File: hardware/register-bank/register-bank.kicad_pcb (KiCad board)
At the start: 2 copper layers, 51.6 x 51.6 mm, 64 parts, among them J1 Conn_Reg, J2 Conn_Power, U1 HEF4557B, U10 74HC251, U11 74HC251, U12 MIC5504-3.3YM5, U13 74LVC1G04, U14 74LVC1G04, U15 74LVC1G04, U16 74LVC1G04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

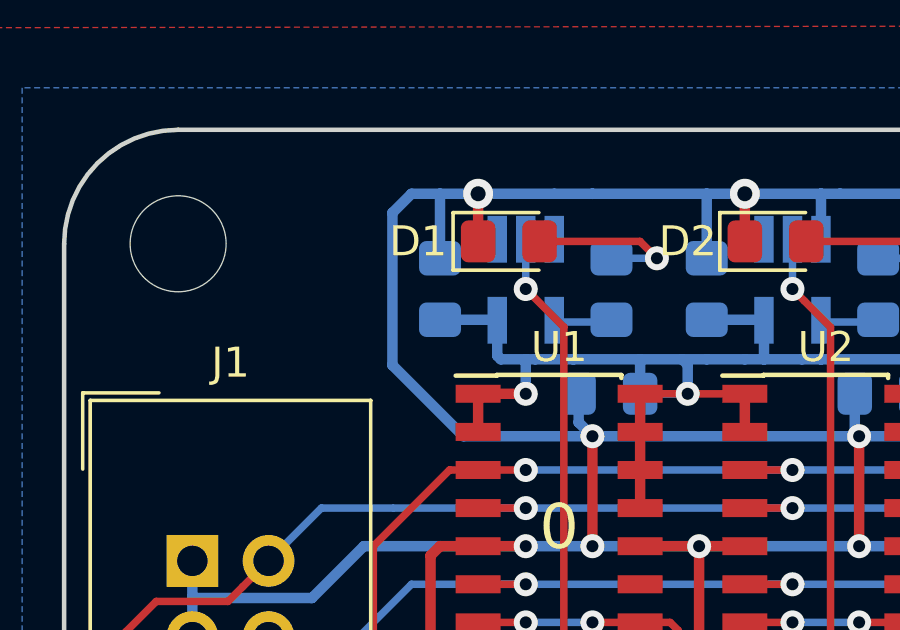
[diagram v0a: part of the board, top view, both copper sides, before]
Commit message: Added test points
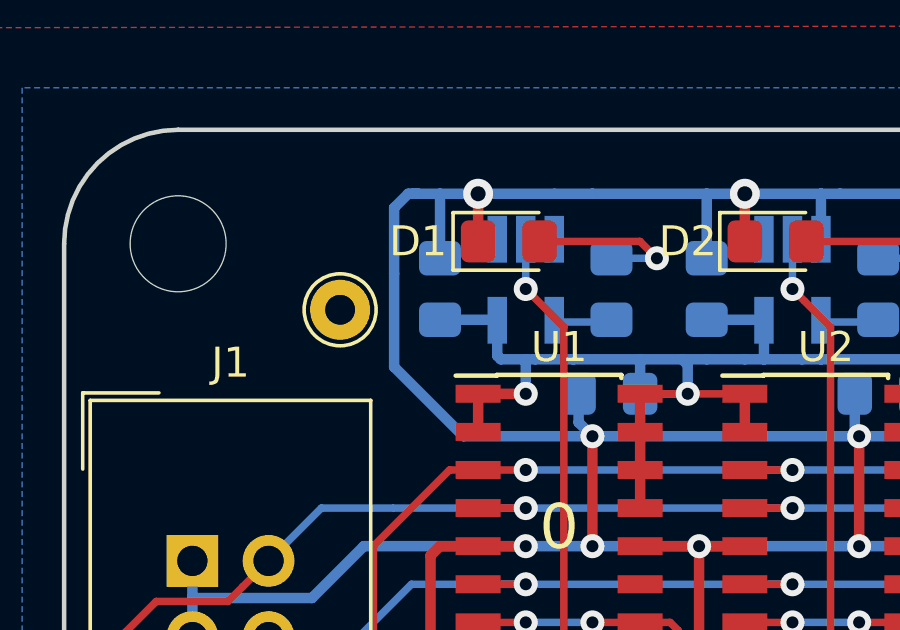
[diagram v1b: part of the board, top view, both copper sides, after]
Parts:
- added TP1: TestPoint, TestPoint:TestPoint_THTPad_D2.0mm_Drill1.0mm, F.Cu at (71.6, 73.4)
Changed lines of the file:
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@@
     (thickness 1.6)
     (drawings 19)
-    (tracks 1025)
+    (tracks 1028)
     (zones 0)
-    (modules 64)
+    (modules 65)
     (nets 72)
   )
@@
   )
   (setup
-    (last_trace_width 0.25)
+    (last_trace_width 0.35)
     (user_trace_width 0.35)
     (user_trace_width 0.5)
@@
       (xy 0.1016 -0.166391)) (layer B.SilkS) (width 0.01))
   )
+  (module TestPoint:TestPoint_THTPad_D2.0mm_Drill1.0mm (layer F.Cu)
+    (at 71.6 73.4)
+    (descr "THT pad as test Point, diameter 2.0mm, hole diameter 1.0mm")
+    (tags "test point THT pad")
+    (attr virtual)
+    (fp_text reference TP1 (at 0 -1.998) (layer F.SilkS) hide
+      (effects (font (size 1 1) (thickness 0.15)))
+    )
+    (fp_text value TestPoint (at 0 2.05) (layer F.Fab)
+      (effects (font (size 1 1) (thickness 0.15)))
+    )
+    (fp_text user %R (at 0 -2) (layer F.Fab)
+      (effects (font (size 1 1) (thickness 0.15)))
+    )
+    (fp_circle (center 0 0) (end 1.5 0) (layer F.CrtYd) (width 0.05))
+    (fp_circle (center 0 0) (end 0 1.2) (layer F.SilkS) (width 0.12))
+    (pad 1 thru_hole circle (at 0 0) (size 2 2) (drill 1) (layers *.Cu *.Mask)
+      (net 1 GND))
+  )
   (gr_text 0 (at 78.9 80.645) (layer F.SilkS)
     (effects (font (size 1.5 1.5) (thickness 0.3)))
@@
   (segment (start 87.6275 71.6075) (end 87.6275 69.535) (width 0.35) (layer B.Cu) (net 1) (status 10))
   (segment (start 87.63 69.5325) (end 88.265 69.5325) (width 0.35) (layer B.Cu) (net 1))
-  (segment (start 75.71 77.615) (end 80.01 77.615) (width 0.35) (layer B.Cu) (net 1))
-  (segment (start 73.3425 75.2475) (end 75.71 77.615) (width 0.35) (layer B.Cu) (net 1))
-  (segment (start 73.3425 70.1675) (end 73.3425 75.2475) (width 0.35) (layer B.Cu) (net 1))
-  (segment (start 74.93 69.5325) (end 73.9775 69.5325) (width 0.35) (layer B.Cu) (net 1))
-  (segment (start 73.9775 69.5325) (end 73.3425 70.1675) (width 0.35) (layer B.Cu) (net 1))
   (segment (start 111.125 76.125) (end 111.05 76.125) (width 0.35) (layer B.Cu) (net 1))
   (segment (start 104.4575 69.5325) (end 103.505 69.5325) (width 0.35) (layer B.Cu) (net 1))
@@
   (segment (start 103.255 93.345) (end 103.1875 93.345) (width 0.5) (layer B.Cu) (net 1))
   (segment (start 103.6 93) (end 103.255 93.345) (width 0.5) (layer B.Cu) (net 1))
+  (segment (start 74.93 69.5325) (end 74.2 69.5325) (width 0.35) (layer B.Cu) (net 1))
+  (segment (start 74.2 69.5325) (end 73.9775 69.5325) (width 0.35) (layer B.Cu) (net 1))
+  (segment (start 73.8675 69.5325) (end 74.2 69.5325) (width 0.35) (layer B.Cu) (net 1))
+  (segment (start 73.4 70) (end 73.8675 69.5325) (width 0.35) (layer B.Cu) (net 1))
+  (segment (start 80.01 77.615) (end 75.71 77.615) (width 0.35) (layer B.Cu) (net 1))
+  (segment (start 75.71 77.615) (end 73.4 75.305) (width 0.35) (layer B.Cu) (net 1))
+  (segment (start 73.4 75.305) (end 73.4 72.2) (width 0.35) (layer B.Cu) (net 1))
+  (segment (start 73.4 72.2) (end 73.4 70) (width 0.35) (layer B.Cu) (net 1))
   (segment (start 81.6 110.49) (end 81.6 109.54) (width 0.25) (layer F.Cu) (net 2) (status 10))
   (segment (start 108.27 76.2) (end 108.27 80.01) (width 0.25) (layer F.Cu) (net 2) (status 30))

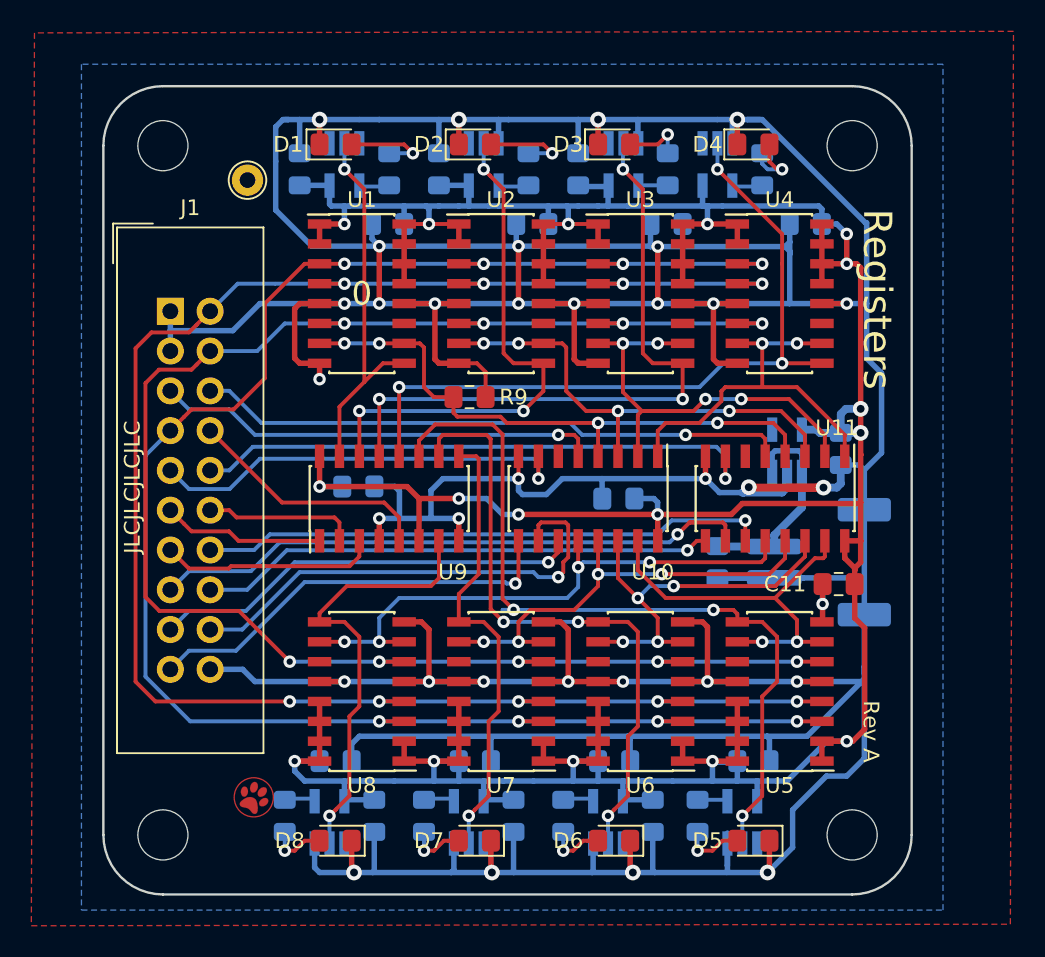
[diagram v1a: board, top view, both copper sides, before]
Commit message: Update all to Kicad 6
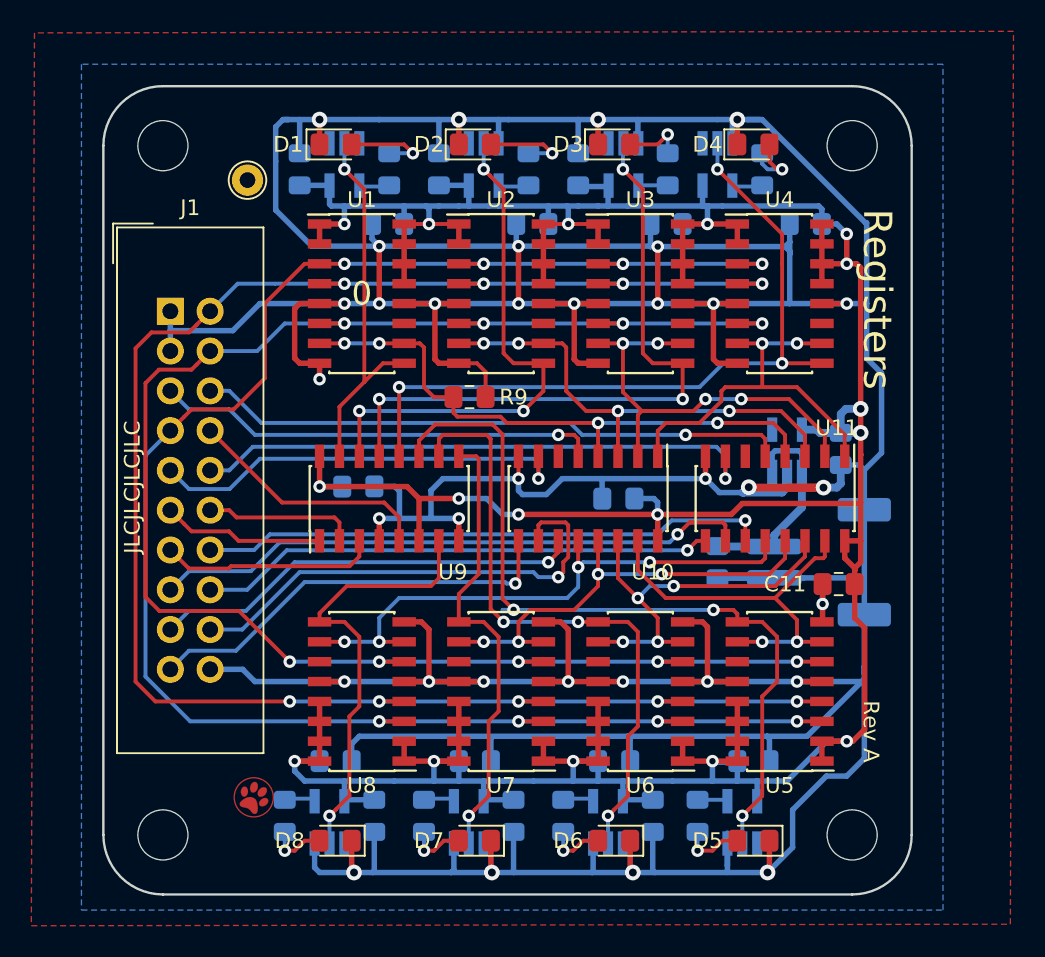
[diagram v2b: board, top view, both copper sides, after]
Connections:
- net /~RIN_EN renamed /~{RIN_EN}
- net /~RIN_EN0 renamed /~{RIN_EN0}
- net /~RIN_EN1 renamed /~{RIN_EN1}
- net /~RIN_EN2 renamed /~{RIN_EN2}
- net /~RIN_EN3 renamed /~{RIN_EN3}
- net /~RIN_EN4 renamed /~{RIN_EN4}
- net /~RIN_EN5 renamed /~{RIN_EN5}
- net /~RIN_EN6 renamed /~{RIN_EN6}
- net /~RIN_EN7 renamed /~{RIN_EN7}
- net /~ROUT_EN_A renamed /~{ROUT_EN_A}
- net /~ROUT_EN_B renamed /~{ROUT_EN_B}
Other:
- net class Default removed
